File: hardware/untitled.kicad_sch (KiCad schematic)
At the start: 0 parts

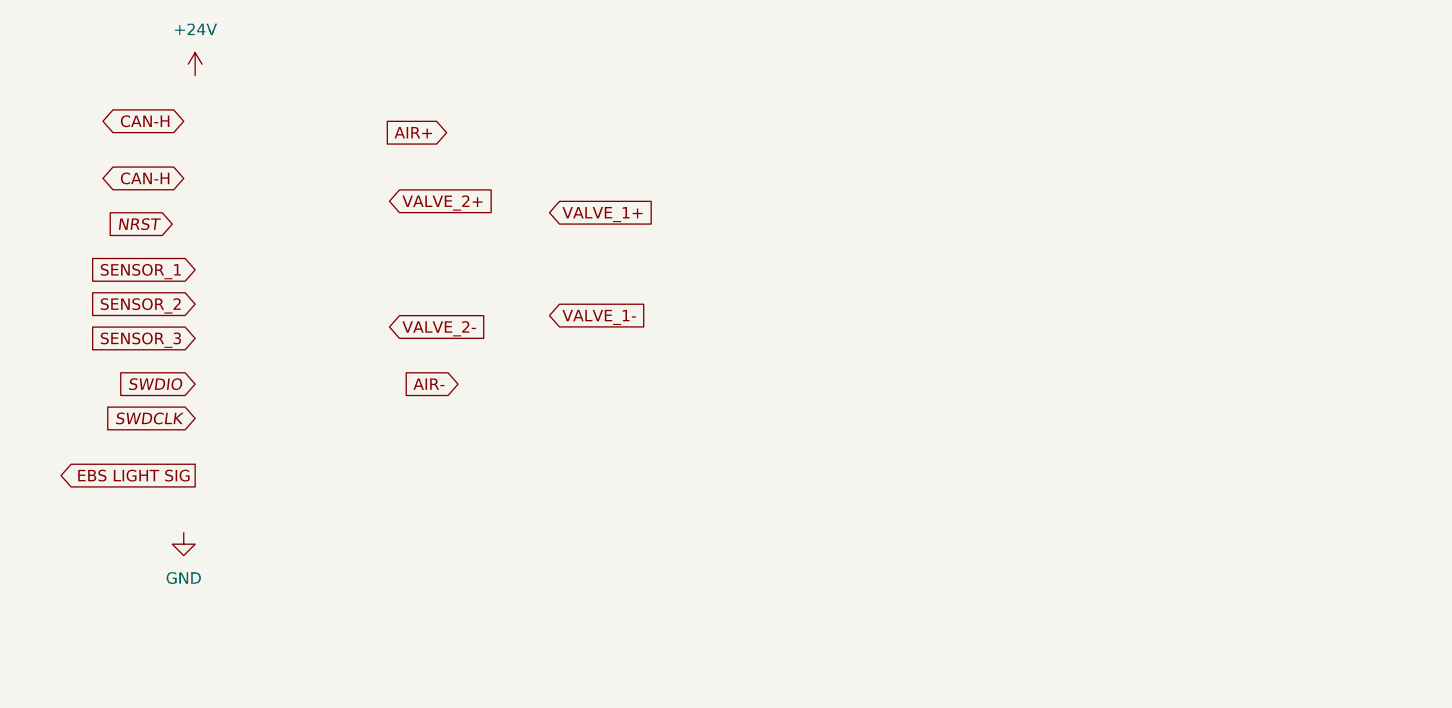
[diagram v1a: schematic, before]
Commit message: Minor changes on v1 schematic
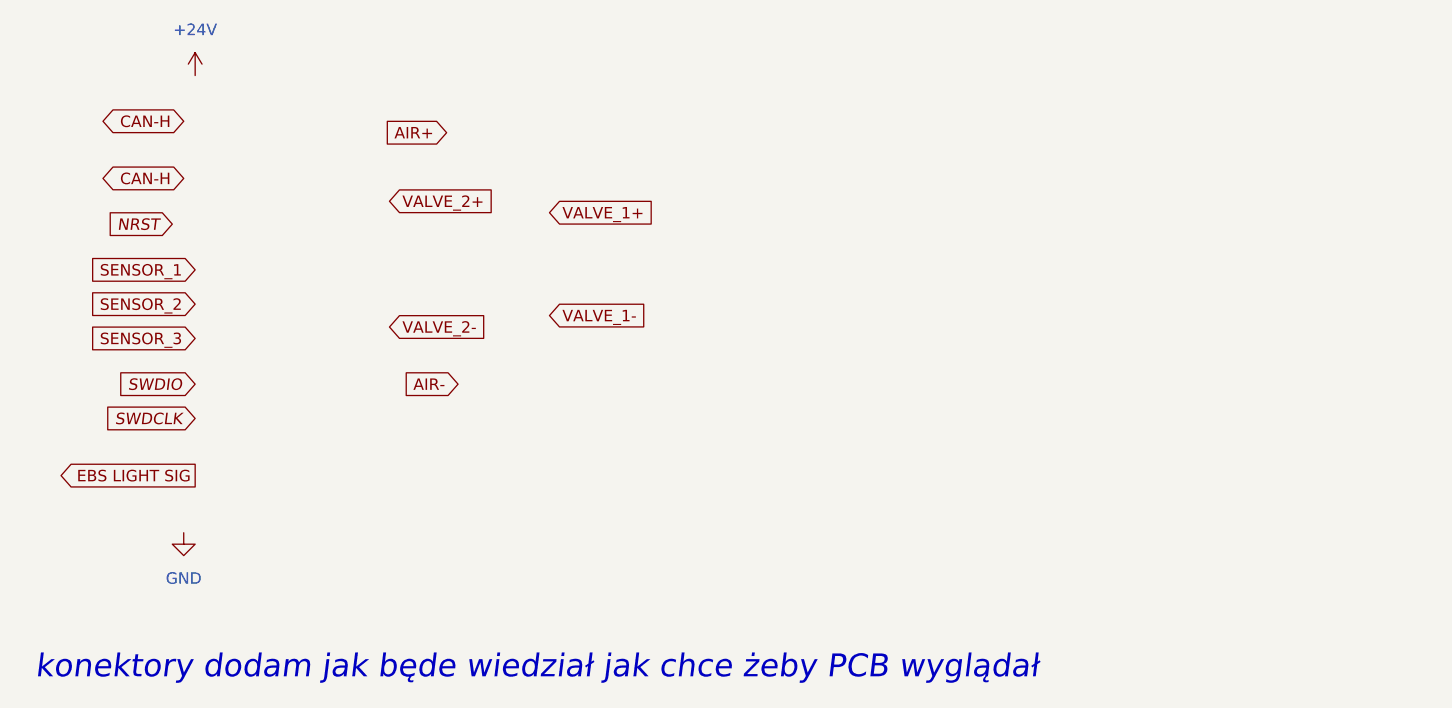
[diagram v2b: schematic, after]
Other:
- note added: "konektory dodam jak będe wiedział jak chce żeby PCB wyglądał"
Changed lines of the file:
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@@
 (kicad_sch (version 20211123) (generator eeschema)
   (paper "A4")
+  (text "konektory dodam jak będe wiedział jak chce żeby PCB wyglądał"
+    (at 93.98 130.81 0)
+    (effects (font (size 2.54 2.54) italic) (justify left bottom))
+  )
   (global_label "SWDIO" (shape input) (at 111.76 97.79 180) (fields_autoplaced)
     (effects (font (size 1.27 1.27) italic) (justify right))
